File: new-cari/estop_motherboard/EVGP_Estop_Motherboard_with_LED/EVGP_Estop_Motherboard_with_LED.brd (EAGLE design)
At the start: 82.6 x 94.1 mm, 48 parts, among them J1 STEERING, J2 DRIVE, J3 JST-XH-03-PIN-LONG-PAD, J4 JST-XH-03-PIN-LONG-PAD, J5 AVR_SPI_PROG_3X2PTH, J6 UX60-MB-5S8, J7 JST-XH-04-PACKAGE-LONG-PAD, Q1 N_FET2, Q2 N_FET1, U1 LM555CMX/NOPBM08A-M, U2 NL27WZ08USG, U3 ATMEGA32U4-AU, X1 TSX-3225 16.0000MF18X-AC0

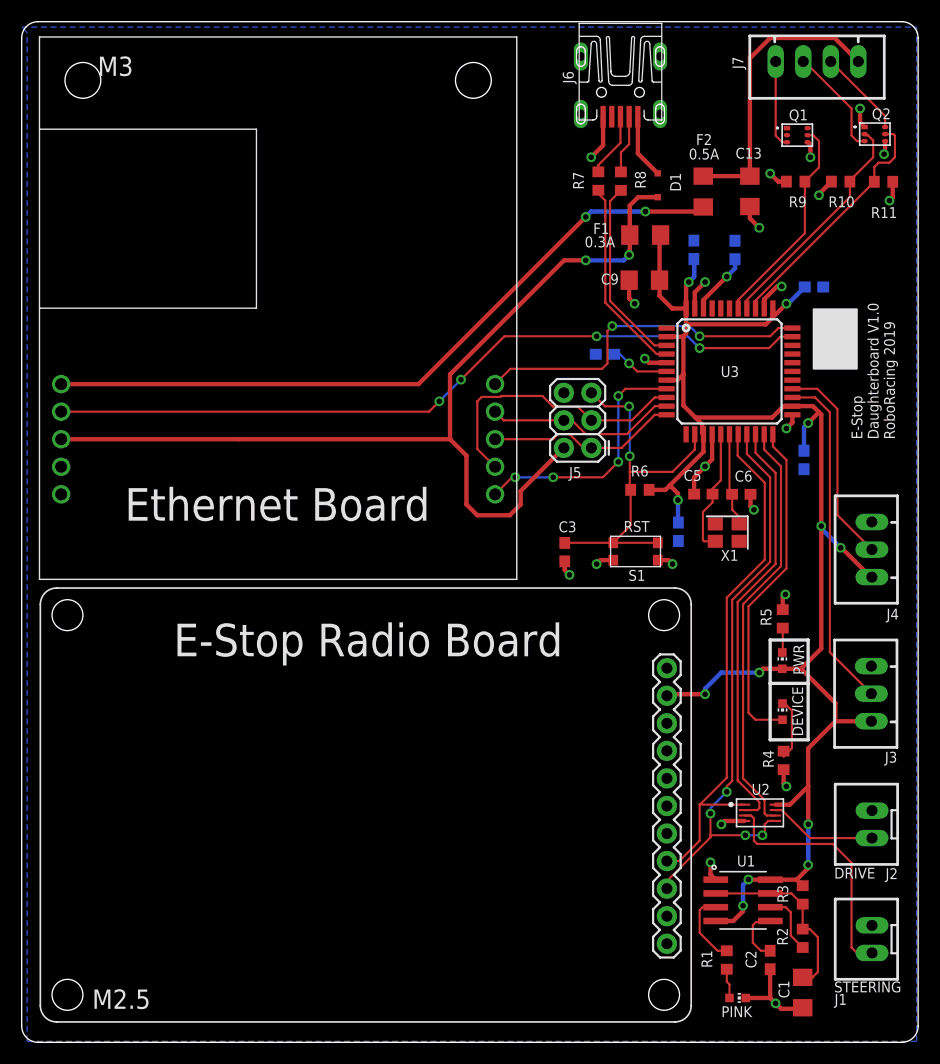
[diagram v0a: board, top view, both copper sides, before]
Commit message: Made small silkscreen changes, moved usb to edge
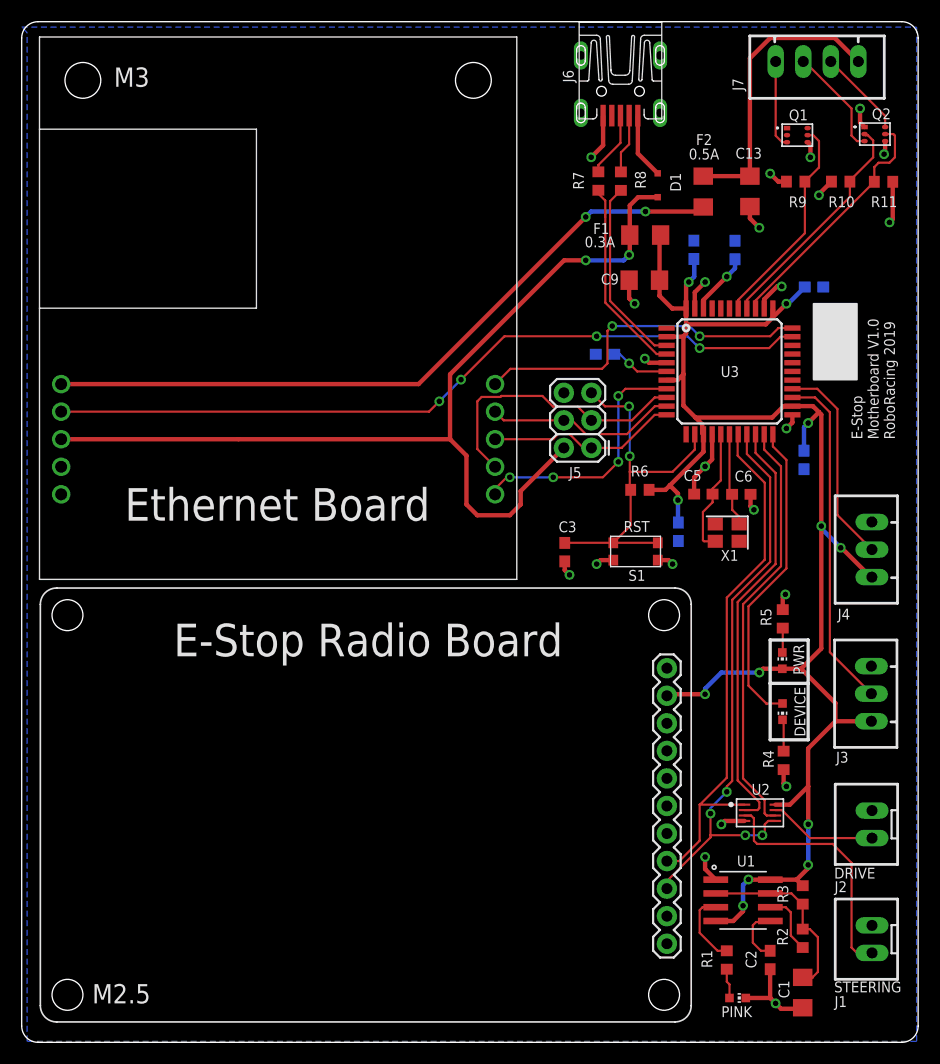
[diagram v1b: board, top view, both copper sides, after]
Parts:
- moved J6 0.10 mm to (61.2, 88.5)
- turned DEVICE to 180 degrees
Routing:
- net N$6: track 6.18 -> 3.13 mm
- net GND: track 56.3 -> 59.1 mm
- net LED1: track 31.0 -> 29.0 mm
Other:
- board text added: "E-Stop Motherboard V1.0 RoboRacing 2019"
- board text removed: "E-Stop Daughterboard V1.0 RoboRacing 2019"
